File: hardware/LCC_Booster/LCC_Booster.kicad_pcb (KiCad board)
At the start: 2 copper layers, 115 x 100 mm, 92 parts, among them J1 A00-216-262-450, J2 Barrel_Jack_MountingPin, J3 Screw_Terminal_01x08, J4 Screw_Terminal_01x02, J5 Screw_Terminal_01x02, Q1 AO3400A, Q2 AO3400A, Q3 AO3400A, Q4 AO3400A, SW1 SW_Push, SW2 SW_Slide_DPDT, U1 ACPL-214-500E, U10 7410, U11 DRV8874PWPR, U12 7410, U13 7410, U14 7410, U15 7410, U16 DRV8874PWPR, U17 7410, U18 7410, U19 7410, U2 7410, U20 7410, U21 DRV8874PWPR, U22 MCP2515-xSO, U23 MCP2562-E-SN, U3 7410, U4 7410, U5 7410, U6 DRV8874PWPR, U7 7410, U8 7410, U9 7410, Y1 16.0 MHz, 22pF

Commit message: Small Tweaks
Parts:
- R1: renamed from R2; footprint Resistor_SMD:R_0815_2038Metric_Pad1.20x4.05mm_HandSolder -> Resistor_SMD:R_01005_0402Metric_Pad0.57x0.30mm_HandSolder
- R10: renamed from R11; footprint Resistor_SMD:R_0815_2038Metric_Pad1.20x4.05mm_HandSolder -> Resistor_SMD:R_01005_0402Metric_Pad0.57x0.30mm_HandSolder
- R11: renamed from R12; footprint Resistor_SMD:R_0815_2038Metric_Pad1.20x4.05mm_HandSolder -> Resistor_SMD:R_01005_0402Metric_Pad0.57x0.30mm_HandSolder
- R12: renamed from R13; footprint Resistor_SMD:R_0815_2038Metric_Pad1.20x4.05mm_HandSolder -> Resistor_SMD:R_01005_0402Metric_Pad0.57x0.30mm_HandSolder
- R2: renamed from R3; footprint Resistor_SMD:R_0815_2038Metric_Pad1.20x4.05mm_HandSolder -> Resistor_SMD:R_01005_0402Metric_Pad0.57x0.30mm_HandSolder
- R3: renamed from R4; footprint Resistor_SMD:R_0815_2038Metric_Pad1.20x4.05mm_HandSolder -> Resistor_SMD:R_01005_0402Metric_Pad0.57x0.30mm_HandSolder
- R4: renamed from R5; footprint Resistor_SMD:R_0815_2038Metric_Pad1.20x4.05mm_HandSolder -> Resistor_SMD:R_01005_0402Metric_Pad0.57x0.30mm_HandSolder
- R5: renamed from R6; footprint Resistor_SMD:R_0815_2038Metric_Pad1.20x4.05mm_HandSolder -> Resistor_SMD:R_01005_0402Metric_Pad0.57x0.30mm_HandSolder
- R6: renamed from R7; footprint Resistor_SMD:R_0815_2038Metric_Pad1.20x4.05mm_HandSolder -> Resistor_SMD:R_01005_0402Metric_Pad0.57x0.30mm_HandSolder
- R7: renamed from R8; footprint Resistor_SMD:R_0815_2038Metric_Pad1.20x4.05mm_HandSolder -> Resistor_SMD:R_01005_0402Metric_Pad0.57x0.30mm_HandSolder
- R8: renamed from R9; footprint Resistor_SMD:R_0815_2038Metric_Pad1.20x4.05mm_HandSolder -> Resistor_SMD:R_01005_0402Metric_Pad0.57x0.30mm_HandSolder
- R9: renamed from R10; footprint Resistor_SMD:R_0815_2038Metric_Pad1.20x4.05mm_HandSolder -> Resistor_SMD:R_01005_0402Metric_Pad0.57x0.30mm_HandSolder
- moved R1 8.82 mm to (47.5, 32.5), turned to -90 degrees
- moved R2 0.52 mm to (45.8, 27.2)
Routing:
- net IOREF: track 573.7 -> 565.0 mm
- net Net-(U6-FAULT_N): track 22.8 -> 14.7 mm
- net /sense_A: track 115.0 -> 110.0 mm
- net Net-(U16-EN_IN1): track 30.9 -> 26.9 mm
- net Net-(Q3-D): track 12.3 -> 13.8 mm
- net /sense_C: track 130.7 -> 132.2 mm
- net Net-(Q2-D): track 10.1 -> 11.5 mm
- net Net-(Q4-D): track 12.3 -> 13.7 mm
- net Net-(U16-PH_IN2): track 30.4 -> 31.6 mm
- net Net-(Q1-D): track 12.3 -> 13.1 mm
- net Net-(U16-FAULT_N): track 28.3 -> 28.9 mm
- net Net-(U11-FAULT_N): track 49.3 -> 50.0 mm
- net /sense_D: track 170.6 -> 171.2 mm
- net /sense_B: track 98.0 -> 98.7 mm
- net Net-(U21-FAULT_N): track 59.0 -> 59.7 mm
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
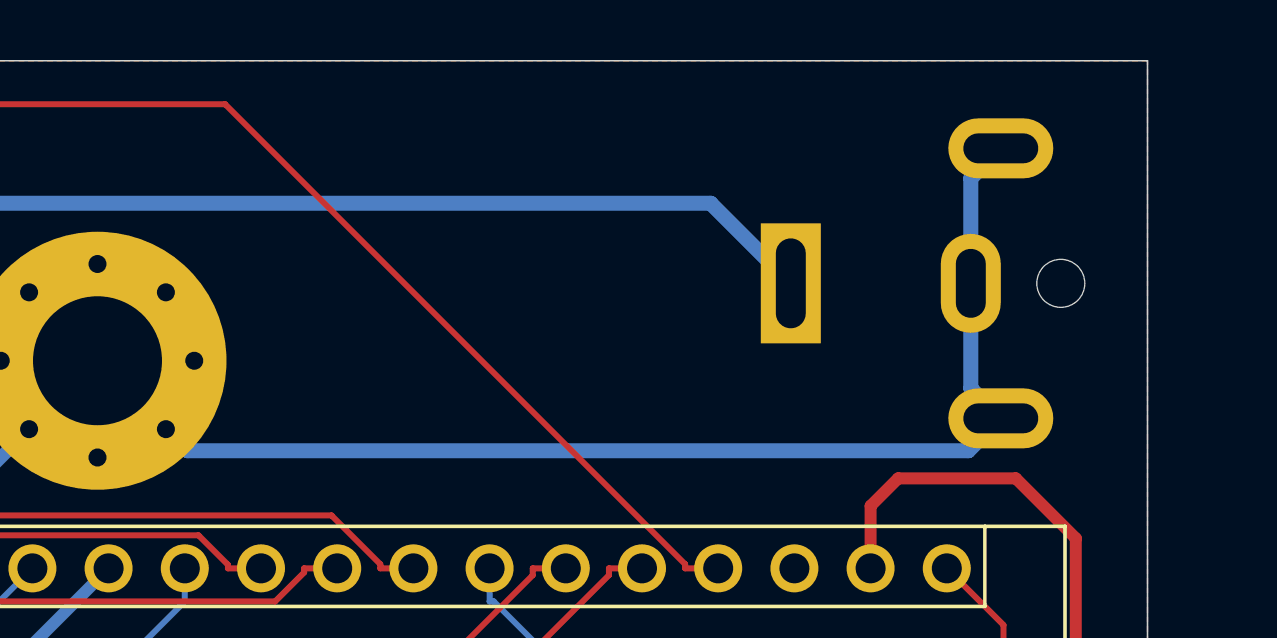
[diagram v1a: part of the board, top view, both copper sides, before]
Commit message: Fixed some footprints
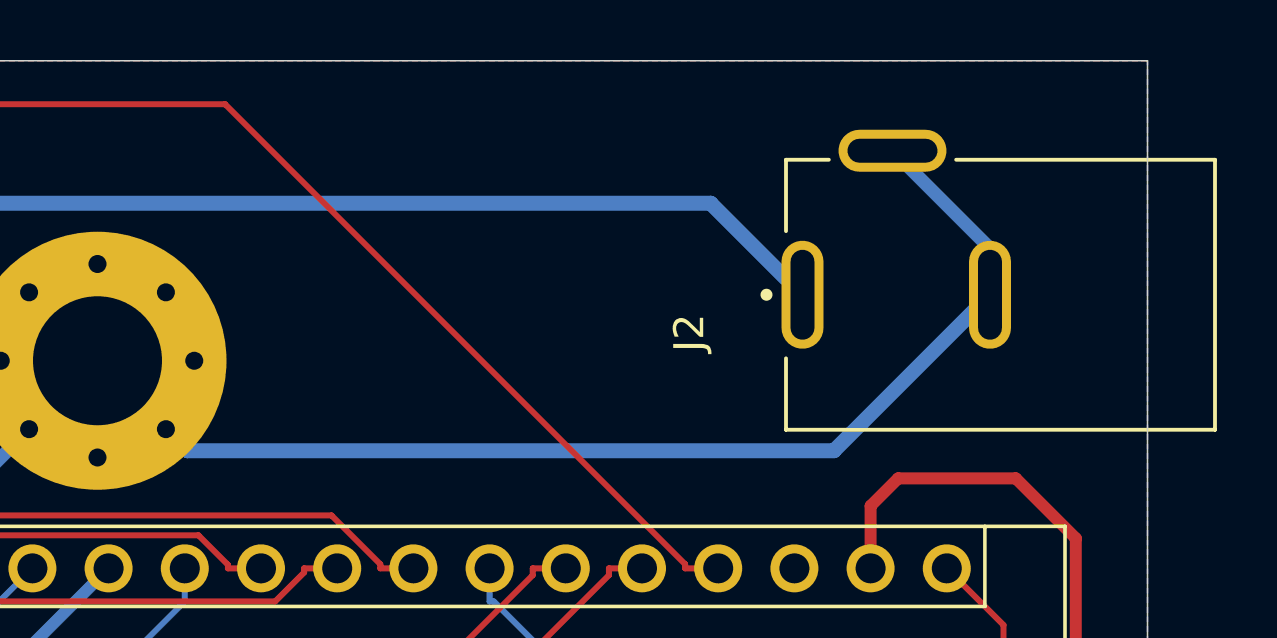
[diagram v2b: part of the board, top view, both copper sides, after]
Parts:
- J2: value Barrel_Jack_MountingPin -> 54-00166; footprint Connector_BarrelJack:BarrelJack_CUI_PJ-063AH_Horizontal -> 54-00166:TENSILITY_54-00166; moved to F.Cu
- moved J2 6.65 mm to (129.8, 27.8), turned to 90 degrees
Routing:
- net GND: track 421.3 -> 419.0 mm
- net VIN: track 41.6 -> 42.1 mm

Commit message: LCC Booster v1.0
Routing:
- net GND: vias 115 -> 125
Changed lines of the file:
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@@
 		(at 129.75 27.8 90)
 		(property "Reference" "J2"
-			(at -1.27 -10.0225 270)
+			(at -1.27 -10.0225 -90)
 			(layer "F.SilkS")
 			(effects
@@
 		)
 		(property "Value" "54-00166"
-			(at 6.985 -8.435 270)
+			(at 6.985 -8.435 -90)
 			(layer "F.Fab")
 			(effects
@@
 	)
 	(via
+		(at 66 60)
+		(size 0.6)
+		(drill 0.3)
+		(layers "F.Cu" "B.Cu")
+		(free yes)
+		(net 5)
+	)
+	(via
 		(at 83.25 54.75)
 		(size 0.6)
@@
 	)
 	(via
+		(at 87.5 91.5)
+		(size 0.6)
+		(drill 0.3)
+		(layers "F.Cu" "B.Cu")
+		(free yes)
+		(net 5)
+	)
+	(via
 		(at 129.25 87)
 		(size 0.6)
@@
 	)
 	(via
+		(at 89.36104 78.725066)
+		(size 0.6)
+		(drill 0.3)
+		(layers "F.Cu" "B.Cu")
+		(free yes)
+		(net 5)
+	)
+	(via
 		(at 70.75 67)
 		(size 0.6)
@@
 	)
 	(via
+		(at 62 59.5)
+		(size 0.6)
+		(drill 0.3)
+		(layers "F.Cu" "B.Cu")
+		(free yes)
+		(net 5)
+	)
+	(via
 		(at 77.25 29.75)
 		(size 0.6)
@@
 	)
 	(via
+		(at 129 57.5)
+		(size 0.6)
+		(drill 0.3)
+		(layers "F.Cu" "B.Cu")
+		(free yes)
+		(net 5)
+	)
+	(via
 		(at 40.75 97.75)
 		(size 1)
@@
 	)
 	(via
+		(at 74.5 67)
+		(size 0.6)
+		(drill 0.3)
+		(layers "F.Cu" "B.Cu")
+		(free yes)
+		(net 5)
+	)
+	(via
 		(at 72.5 61.75)
 		(size 0.6)
@@
 	)
 	(via
+		(at 78.47928 59.518645)
+		(size 0.6)
+		(drill 0.3)
+		(layers "F.Cu" "B.Cu")
+		(free yes)
+		(net 5)
+	)
+	(via
 		(at 88.75 73.25)
 		(size 0.6)
@@
 	)
 	(via
+		(at 88.85677 70.740688)
+		(size 0.6)
+		(drill 0.3)
+		(layers "F.Cu" "B.Cu")
+		(free yes)
+		(net 5)
+	)
+	(via
 		(at 84.25 32.25)
 		(size 1)
@@
 	)
 	(via
+		(at 68 111.5)
+		(size 0.6)
+		(drill 0.3)
+		(layers "F.Cu" "B.Cu")
+		(free yes)
+		(net 5)
+	)
+	(via
 		(at 67.5 104.75)
 		(size 0.6)
@@
 	)
 	(via
+		(at 90.182202 81.687909)
+		(size 0.6)
+		(drill 0.3)
+		(layers "F.Cu" "B.Cu")
+		(free yes)
+		(net 5)
+	)
+	(via
 		(at 90 51.75)
 		(size 0.6)
@@
 			(thermal_bridge_width 0.5)
 			(island_removal_mode 2)
-			(island_area_min 8)
+			(island_area_min 5)
 		)
 		(polygon

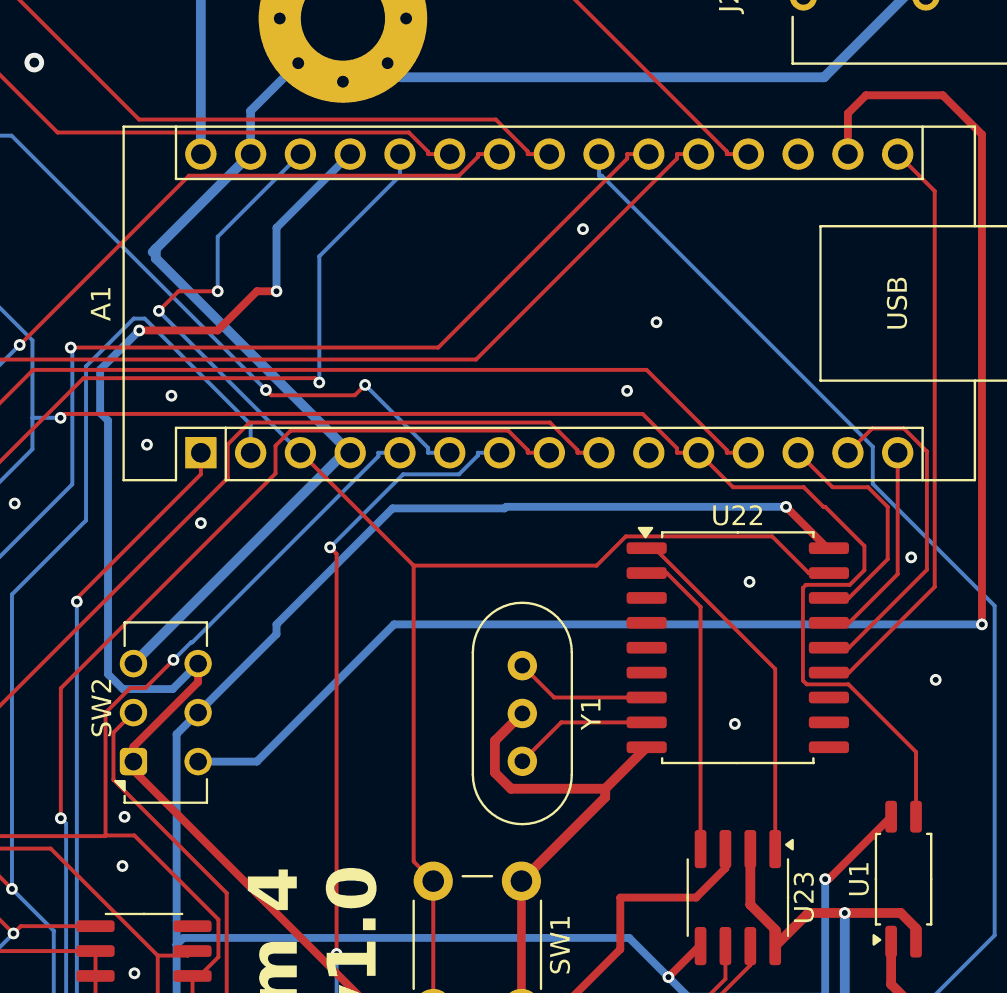
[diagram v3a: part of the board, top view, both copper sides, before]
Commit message: LCC Command Station Shield
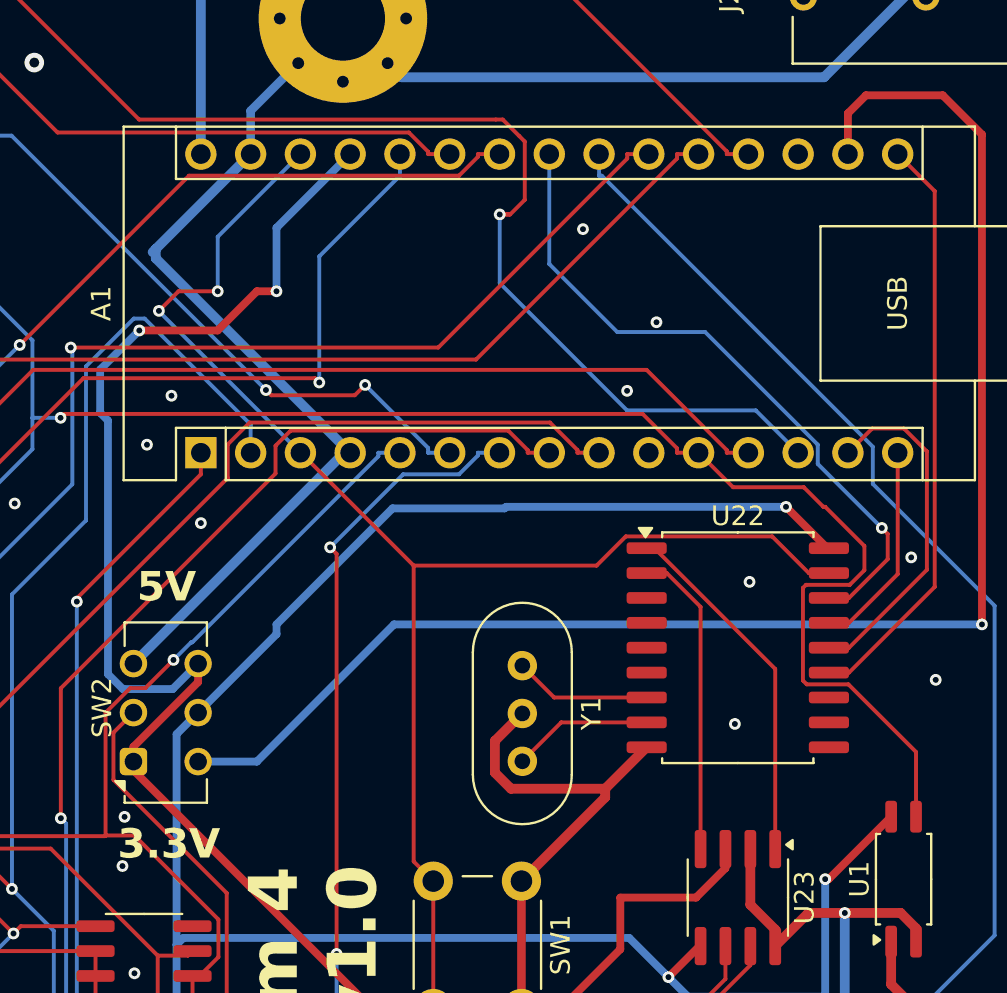
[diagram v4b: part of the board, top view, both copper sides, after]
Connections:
- A1 pad 13: /cs -> /dir_A
- A1 pad 23: /dir_A -> /cs
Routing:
- net /dir_A: track 76.5 -> 102.2 mm, vias 3 -> 4
- net /cs: track 12.2 -> 34.3 mm, vias 0 -> 1
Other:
- board text added: "3.3V"
- board text added: "5V"
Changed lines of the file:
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@@
 			(layers "*.Cu" "*.Mask")
 			(remove_unused_layers no)
-			(net 15 "/cs")
+			(net 20 "/dir_A")
 			(pinfunction "D10")
 			(pintype "bidirectional")
@@
 			(layers "*.Cu" "*.Mask")
 			(remove_unused_layers no)
-			(net 20 "/dir_A")
+			(net 15 "/cs")
 			(pinfunction "A4")
 			(pintype "bidirectional")
@@
 		)
 	)
+	(gr_text "3.3V"
+		(at 88.5 73 0)
+		(layer "F.SilkS")
+		(effects
+			(font
+				(size 1.5 1.5)
+				(thickness 0.3)
+				(bold yes)
+			)
+			(justify left bottom)
+		)
+	)
 	(gr_text "A-"
 		(at 33 56.75 0)
@@
 		)
 	)
+	(gr_text "5V"
+		(at 91 59 0)
+		(layer "F.SilkS")
+		(effects
+			(font
+				(size 1.5 1.5)
+				(thickness 0.3)
+				(bold yes)
+			)
+		)
+	)
 	(gr_text "DCC+"
 		(at 22.25 105.5 0)
@@
 	)
 	(segment
-		(start 127.8 54.92)
-		(end 127.8 57.595)
+		(start 127.8 56.3)
+		(end 127.5 56)
 		(width 0.2)
 		(layer "F.Cu")
@@
 	(segment
 		(start 127.8 57.595)
-		(end 125.825 59.57)
+		(end 127.8 56.3)
 		(width 0.2)
 		(layer "F.Cu")
@@
 	)
 	(segment
-		(start 124.99 53.92)
-		(end 126.8 53.92)
+		(start 125.825 59.57)
+		(end 124.8 59.57)
 		(width 0.2)
 		(layer "F.Cu")
@@
 	)
 	(segment
-		(start 123.23 52.16)
-		(end 124.99 53.92)
+		(start 127.8 57.595)
+		(end 125.825 59.57)
 		(width 0.2)
 		(layer "F.Cu")
 		(net 15)
 	)
+	(via
+		(at 127.5 56)
+		(size 0.6)
+		(drill 0.3)
+		(layers "F.Cu" "B.Cu")
+		(net 15)
+	)
 	(segment
-		(start 126.8 53.92)
-		(end 127.8 54.92)
+		(start 114 46)
+		(end 110.53 42.53)
 		(width 0.2)
-		(layer "F.Cu")
+		(layer "B.Cu")
 		(net 15)
 	)
 	(segment
-		(start 125.825 59.57)
-		(end 124.8 59.57)
+		(start 127.5 56)
+		(end 124.23 52.73)
 		(width 0.2)
-		(layer "F.Cu")
+		(layer "B.Cu")
+		(net 15)
+	)
+	(segment
+		(start 110.53 42.53)
+		(end 110.53 36.92)
+		(width 0.2)
+		(layer "B.Cu")
+		(net 15)
+	)
+	(segment
+		(start 118.484214 46)
+		(end 114 46)
+		(width 0.2)
+		(layer "B.Cu")
+		(net 15)
+	)
+	(segment
+		(start 124.23 52.73)
+		(end 124.23 51.745786)
+		(width 0.2)
+		(layer "B.Cu")
+		(net 15)
+	)
+	(segment
+		(start 124.23 51.745786)
+		(end 118.484214 46)
+		(width 0.2)
+		(layer "B.Cu")
 		(net 15)
 	)
@@
 	)
 	(segment
+		(start 109.27835 39.255153)
+		(end 108.533503 40)
+		(width 0.2)
+		(layer "F.Cu")
+		(net 20)
+	)
+	(segment
 		(start 79.7 27.2514)
 		(end 77.4374 27.2514)
@@
 	)
 	(segment
-		(start 109.428 36.92)
-		(end 110.53 36.92)
+		(start 108.1563 35.1563)
+		(end 109 36)
 		(width 0.2)
 		(layer "F.Cu")
@@
 	)
 	(segment
-		(start 107.802 35.1563)
-		(end 109.428 36.7823)
+		(start 61.7395 28.2582)
+		(end 61.7395 27.5429)
 		(width 0.2)
 		(layer "F.Cu")
@@
 	)
 	(segment
-		(start 61.7395 28.2582)
-		(end 61.7395 27.5429)
+		(start 108 40)
+		(end 108.5 40)
 		(width 0.2)
 		(layer "F.Cu")
@@
 	)
 	(segment
+		(start 109 36)
+		(end 109.27835 36.27835)
+		(width 0.2)
+		(layer "F.Cu")
+		(net 20)
+	)
+	(segment
 		(start 81.9812 27.54)
 		(end 89.5975 35.1563)
@@
 	)
 	(segment
-		(start 109.428 36.7823)
-		(end 109.428 36.92)
+		(start 62.4444 42.7094)
+		(end 61.2913 42.7094)
 		(width 0.2)
 		(layer "F.Cu")
@@
 	)
 	(segment
-		(start 62.4444 42.7094)
-		(end 61.2913 42.7094)
+		(start 108.533503 40)
+		(end 108 40)
+		(width 0.2)
+		(layer "F.Cu")
+		(net 20)
+	)
+	(segment
+		(start 107.802 35.1563)
+		(end 108.1563 35.1563)
 		(width 0.2)
 		(layer "F.Cu")
@@
 		(net 20)
 	)
+	(segment
+		(start 109.27835 36.27835)
+		(end 109.27835 39.255153)
+		(width 0.2)
+		(layer "F.Cu")
+		(net 20)
+	)
+	(via
+		(at 108 40)
+		(size 0.6)
+		(drill 0.3)
+		(layers "F.Cu" "B.Cu")
+		(net 20)
+	)
 	(via
 		(at 61.7395 28.2582)
@@
 	)
 	(segment
+		(start 108 40)
+		(end 108 43.5)
+		(width 0.2)
+		(layer "B.Cu")
+		(net 20)
+	)
+	(segment
 		(start 77.3247 27.1387)
 		(end 62.859 27.1387)
@@
 	)
 	(segment
+		(start 121.07 50)
+		(end 123.23 52.16)
+		(width 0.2)
+		(layer "B.Cu")
+		(net 20)
+	)
+	(segment
 		(start 62.859 27.1387)
 		(end 61.7395 28.2582)
 		(width 0.2)
 		(layer "B.Cu")
+		(net 20)
+	)
+	(segment
+		(start 114.5 50)
+		(end 121.07 50)
+		(width 0.2)
+		(layer "B.Cu")
+		(net 20)
+	)
+	(segment
+		(start 108 43.5)
+		(end 114.5 50)
+		(width 0.2)
+		(layer "B.Cu")
